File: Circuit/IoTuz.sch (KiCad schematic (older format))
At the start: 35 parts, among them P1 SD_SPI, P2 BATTERY, P3 USB_5PIN_SHELL, P4 LED_1, P5 LED_2, P6 CONN_01X20, P7 CONN_01X20, P8 LCD_SCREEN, Q1 S8050, Q2 S8050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

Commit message: Moved LXDC2XQ location
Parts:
- P8: footprint (none) -> libs:QDTech-3.2in-TFT
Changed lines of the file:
@@
 F 0 "P8" H 9150 4250 50  0000 C CNN
 F 1 "LCD_SCREEN" V 9250 3500 50  0000 C CNN
-F 2 "" H 9150 3500 50  0001 C CNN
+F 2 "libs:QDTech-3.2in-TFT" H 9150 3500 50  0001 C CNN
 F 3 "" H 9150 3500 50  0000 C CNN
 	1    9150 3500

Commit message: Added footprint for LCD.
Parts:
- removed P1: SD_SPI, symbol CONN_01X04
- removed P8: LCD_SCREEN, libs:QDTech-3.2in-TFT, symbol CONN_01X14
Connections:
- net labels removed: CS, D/C, LED, RESET, SCK, SDI(MOSI), SDO(MISO), SD_CS, SD_MISO, SD_MOSI, SD_SCK, T_CLK, T_CS, T_DIN, T_DO, T_IRQ
- wire segments 232 -> 213
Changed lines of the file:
@@
 LIBS:bme280
 LIBS:lxdc2xq
+LIBS:qdtech-3.2-tft
 LIBS:IoTuz-cache
 EELAYER 25 0
@@
 Wire Wire Line
 	2250 2150 2250 1500
-$Comp
-L CONN_01X14 P8
-U 1 1 581185F0
-P 9150 3500
-F 0 "P8" H 9150 4250 50  0000 C CNN
-F 1 "LCD_SCREEN" V 9250 3500 50  0000 C CNN
-F 2 "libs:QDTech-3.2in-TFT" H 9150 3500 50  0001 C CNN
-F 3 "" H 9150 3500 50  0000 C CNN
-	1    9150 3500
-	-1   0    0    -1
-$EndComp
-$Comp
-L CONN_01X04 P1
-U 1 1 58119106
-P 9150 2350
-F 0 "P1" H 9150 2600 50  0000 C CNN
-F 1 "SD_SPI" V 9250 2350 50  0000 C CNN
-F 2 "" H 9150 2350 50  0001 C CNN
-F 3 "" H 9150 2350 50  0000 C CNN
-	1    9150 2350
-	-1   0    0    -1
-$EndComp
-Wire Wire Line
-	9350 2200 9800 2200
-Text Label 9800 2200 2    60   ~ 0
-SD_CS
-Wire Wire Line
-	9350 2300 9800 2300
-Wire Wire Line
-	9800 2400 9350 2400
-Wire Wire Line
-	9800 2500 9350 2500
-Text Label 9800 2300 2    60   ~ 0
-SD_MOSI
-Text Label 9800 2400 2    60   ~ 0
-SD_MISO
-Text Label 9800 2500 2    60   ~ 0
-SD_SCK
-Wire Wire Line
-	9350 2850 9800 2850
-Wire Wire Line
-	9350 2950 9800 2950
-Wire Wire Line
-	9350 3050 9800 3050
-Wire Wire Line
-	9350 3150 9800 3150
-Wire Wire Line
-	9350 3250 9800 3250
-Wire Wire Line
-	9350 3350 9800 3350
-Wire Wire Line
-	9350 3450 9800 3450
-Wire Wire Line
-	9350 3550 9800 3550
-Wire Wire Line
-	9350 3650 9800 3650
-Wire Wire Line
-	9350 3750 9800 3750
-Wire Wire Line
-	9350 3850 9800 3850
-Wire Wire Line
-	9350 3950 9800 3950
-Wire Wire Line
-	9350 4150 9650 4150
-Text Label 9800 2850 2    60   ~ 0
-T_IRQ
-Text Label 9800 2950 2    60   ~ 0
-T_DO
-Text Label 9800 3050 2    60   ~ 0
-T_DIN
-Text Label 9800 3150 2    60   ~ 0
-T_CS
-Text Label 9800 3250 2    60   ~ 0
-T_CLK
-Text Label 9800 3350 2    60   ~ 0
-SDO(MISO)
-Text Label 9800 3450 2    60   ~ 0
-LED
-Text Label 9800 3550 2    60   ~ 0
-SCK
-Text Label 9800 3650 2    60   ~ 0
-SDI(MOSI)
-Text Label 9800 3750 2    60   ~ 0
-D/C
-Text Label 9800 3850 2    60   ~ 0
-RESET
-Text Label 9800 3950 2    60   ~ 0
-CS
-$Comp
-L GND #PWR030
-U 1 1 58121E66
-P 9500 4250
-F 0 "#PWR030" H 9500 4000 50  0001 C CNN
-F 1 "GND" H 9500 4100 50  0000 C CNN
-F 2 "" H 9500 4250 50  0000 C CNN
-F 3 "" H 9500 4250 50  0000 C CNN
-	1    9500 4250
-	1    0    0    -1
-$EndComp
-$Comp
-L +3.3V #PWR031
-U 1 1 58121F10
-P 9650 4150
-F 0 "#PWR031" H 9650 4000 50  0001 C CNN
-F 1 "+3.3V" H 9650 4290 50  0000 C CNN
-F 2 "" H 9650 4150 50  0000 C CNN
-F 3 "" H 9650 4150 50  0000 C CNN
-	1    9650 4150
-	1    0    0    -1
-$EndComp
-Wire Wire Line
-	9350 4050 9500 4050
-Wire Wire Line
-	9500 4050 9500 4250
 $Sheet
 S 1000 3850 850  500
@@
 $EndSheet
 $Sheet
-S 7300 3700 1100 1300
+S 9300 3300 1100 1300
 U 5811E13F
 F0 "LCDTouch" 60

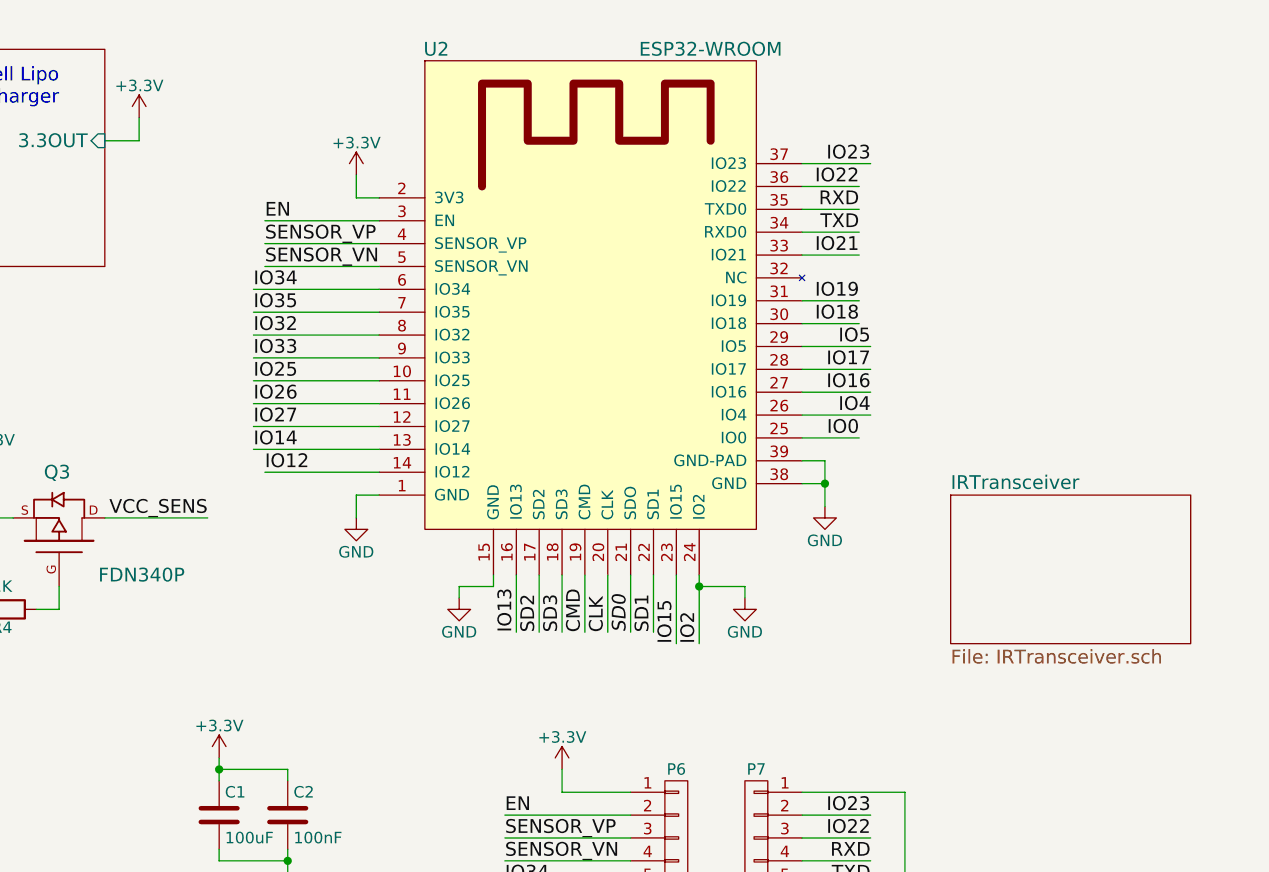
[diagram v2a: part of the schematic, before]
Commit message: Markup IO allocation & add some datasheets.
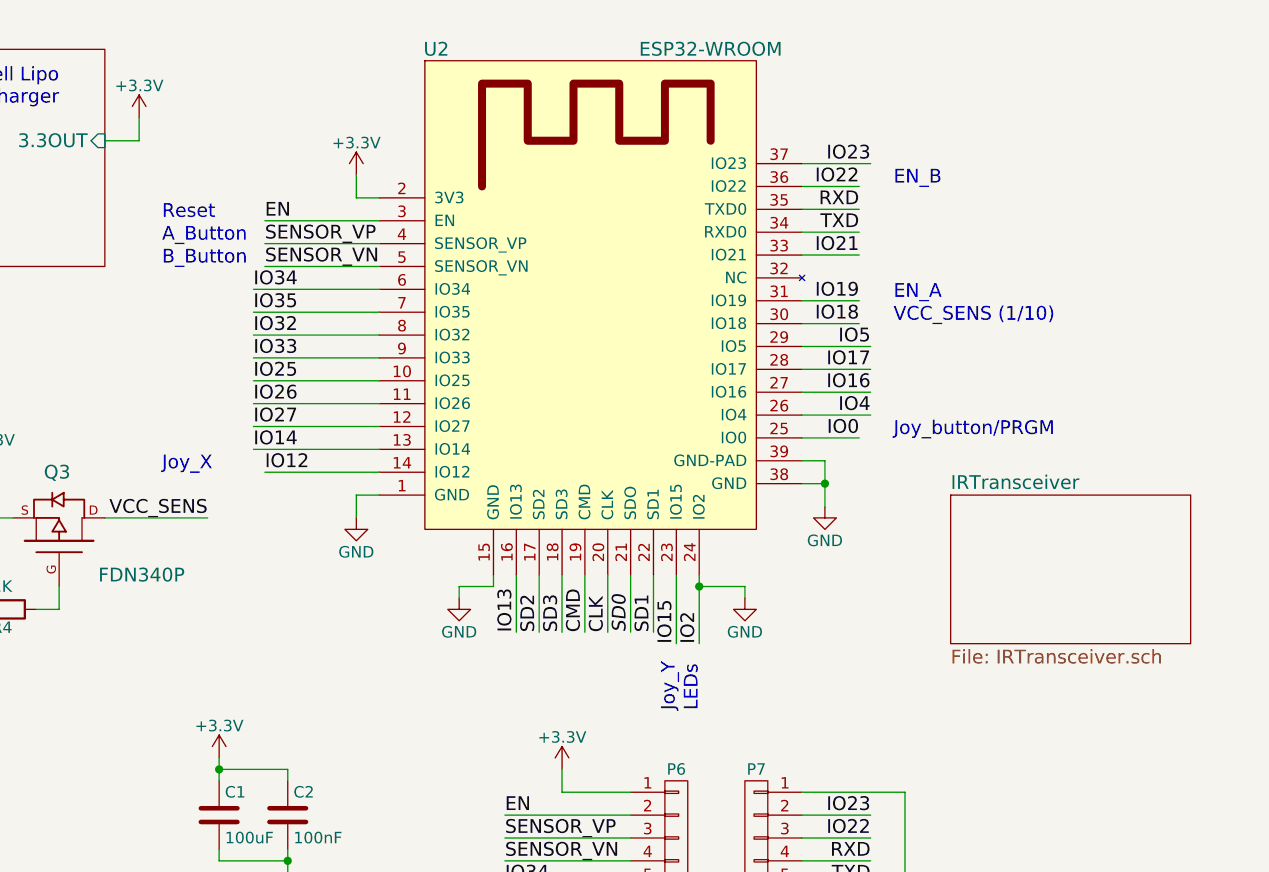
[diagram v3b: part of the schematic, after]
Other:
- note added: "A_Button"
- note added: "B_Button"
- note added: "EN_A"
- note added: "EN_B"
- note added: "Joy_X"
- note added: "Joy_Y"
- note added: "Joy_button/PRGM"
- note added: "LEDs"
- note added: "Reset"
- note added: "VCC_SENS (1/10)"
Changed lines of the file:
@@
 F1 "IRTransceiver.sch" 60
 $EndSheet
+Text Notes 7050 2350 0    60   ~ 0
+Joy_button/PRGM
+Text Notes 7050 1750 0    60   ~ 0
+EN_A
+Text Notes 7050 1250 0    60   ~ 0
+EN_B
+Text Notes 3850 2500 0    60   ~ 0
+Joy_X
+Text Notes 6100 3550 1    60   ~ 0
+Joy_Y
+Text Notes 7050 1850 0    60   ~ 0
+VCC_SENS (1/10)
+Text Notes 3850 1500 0    60   ~ 0
+A_Button
+Text Notes 3850 1600 0    60   ~ 0
+B_Button
+Text Notes 3850 1400 0    60   ~ 0
+Reset
+Text Notes 6200 3550 1    60   ~ 0
+LEDs
 $EndSCHEMATC

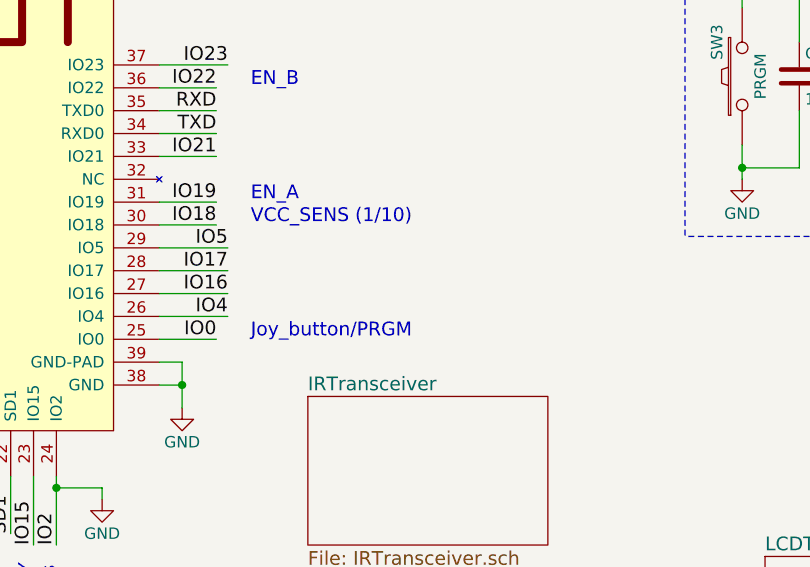
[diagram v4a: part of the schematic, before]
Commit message: Audio choices being narrowed.
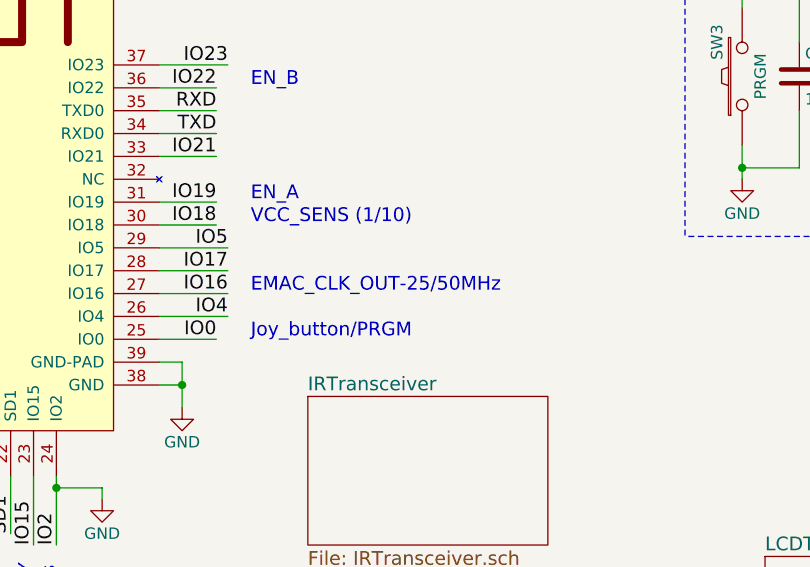
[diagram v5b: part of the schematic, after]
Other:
- note added: "EMAC_CLK_OUT-25/50MHz"
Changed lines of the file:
@@
 Text Notes 6200 3550 1    60   ~ 0
 LEDs
+Text Notes 7050 2150 0    60   ~ 0
+EMAC_CLK_OUT-25/50MHz
 $EndSCHEMATC

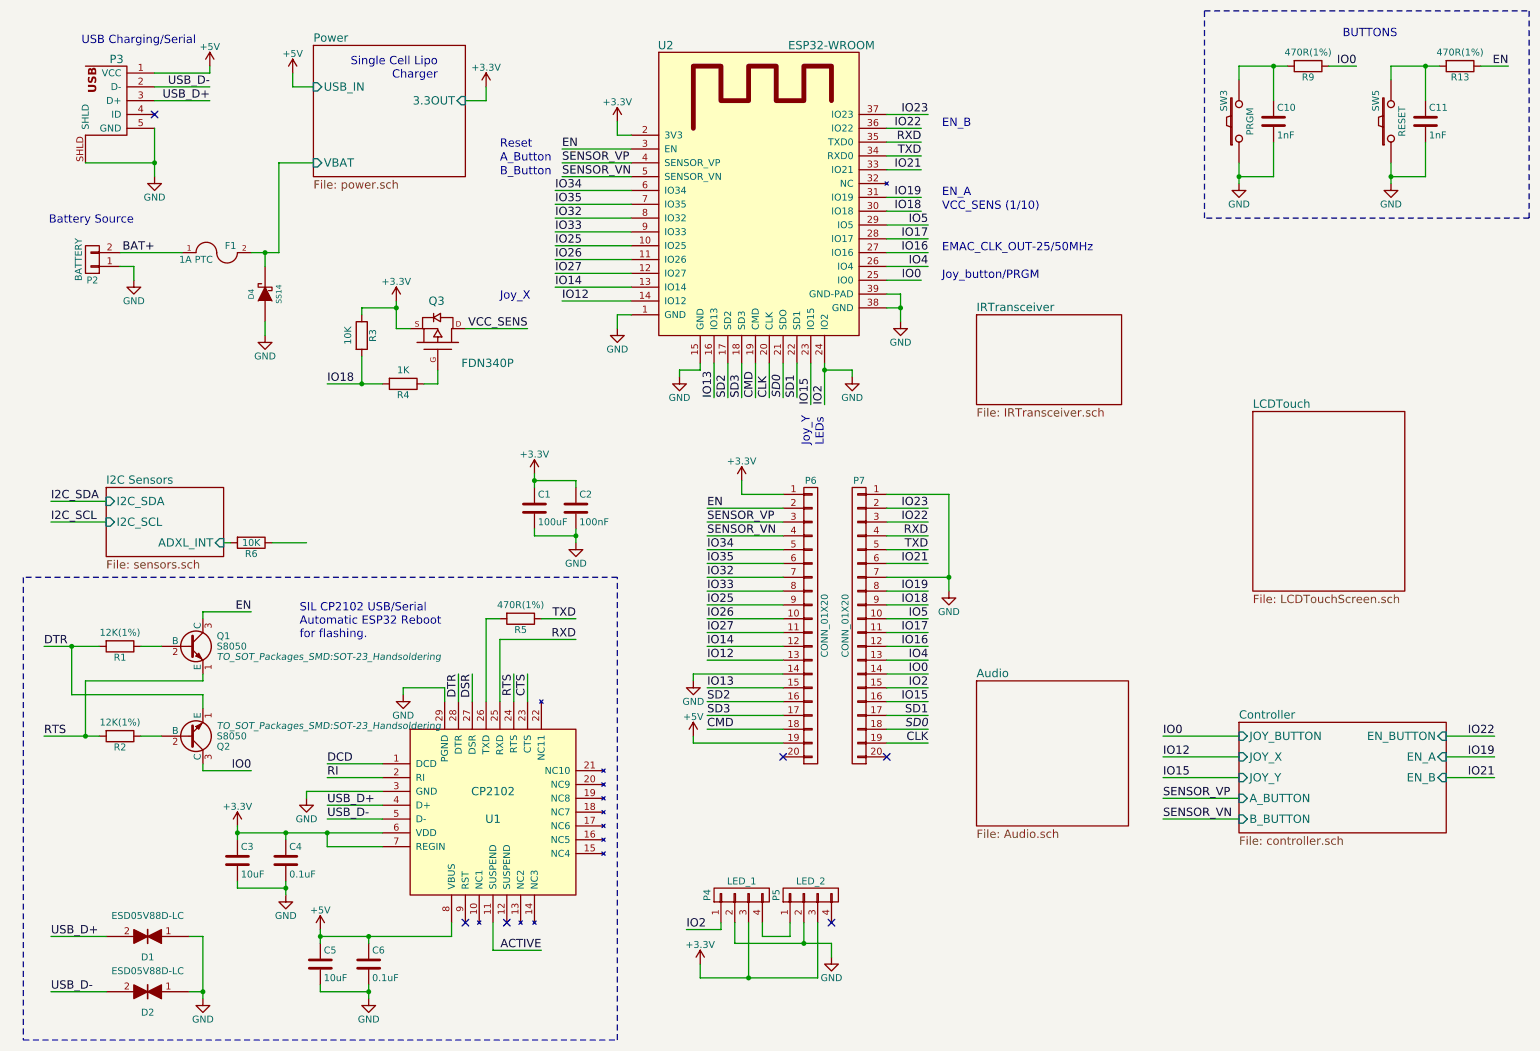
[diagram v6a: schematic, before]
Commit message: Audio hierarchical pins.
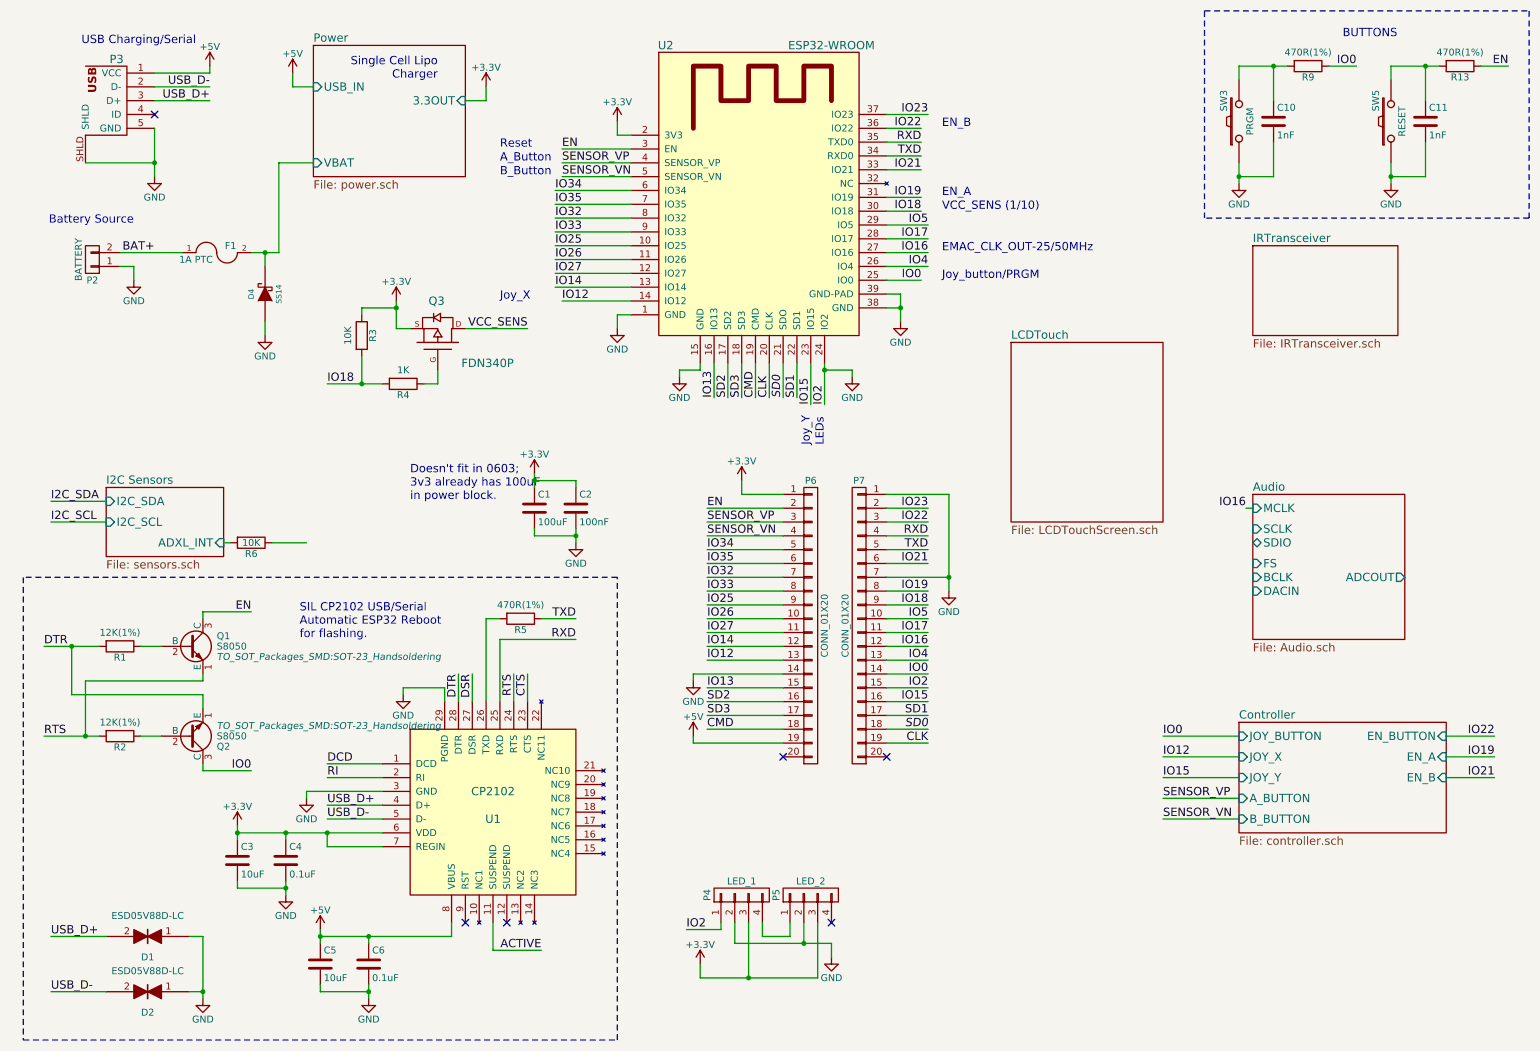
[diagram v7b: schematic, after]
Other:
- note added: "Doesn't fit in 0603;\n3v3 already has 100uF\nin power block."
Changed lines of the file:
@@
 	10700 5950 11050 5950
 $Sheet
-S 7300 5250 1100 1050
+S 9300 3900 1100 1050
 U 5811BE75
 F0 "Audio" 60
 F1 "Audio.sch" 60
+F2 "MCLK" I L 9300 4000 60
+F3 "SCLK" I L 9300 4150 60
+F4 "SDIO" B L 9300 4250 60
+F5 "FS" I L 9300 4400 60
+F6 "BCLK" I L 9300 4500 60
+F7 "DACIN" I L 9300 4600 60
+F8 "ADCOUT" O R 10400 4500 60
 $EndSheet
 $Sheet
-S 9300 3300 1100 1300
+S 7550 2800 1100 1300
 U 5811E13F
 F0 "LCDTouch" 60
@@
 $EndSheet
 $Sheet
-S 7300 2600 1050 650
+S 9300 2100 1050 650
 U 5811E5C9
 F0 "IRTransceiver" 60
@@
 Text Notes 7050 2150 0    60   ~ 0
 EMAC_CLK_OUT-25/50MHz
+Text Notes 3200 3950 0    60   ~ 0
+Doesn't fit in 0603;\n3v3 already has 100uF\nin power block.
+Text Label 9250 4000 2    60   ~ 0
+IO16
+Wire Wire Line
+	9250 4000 9300 4000
 $EndSCHEMATC

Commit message: Removed duplicate stabilizing capacitors.
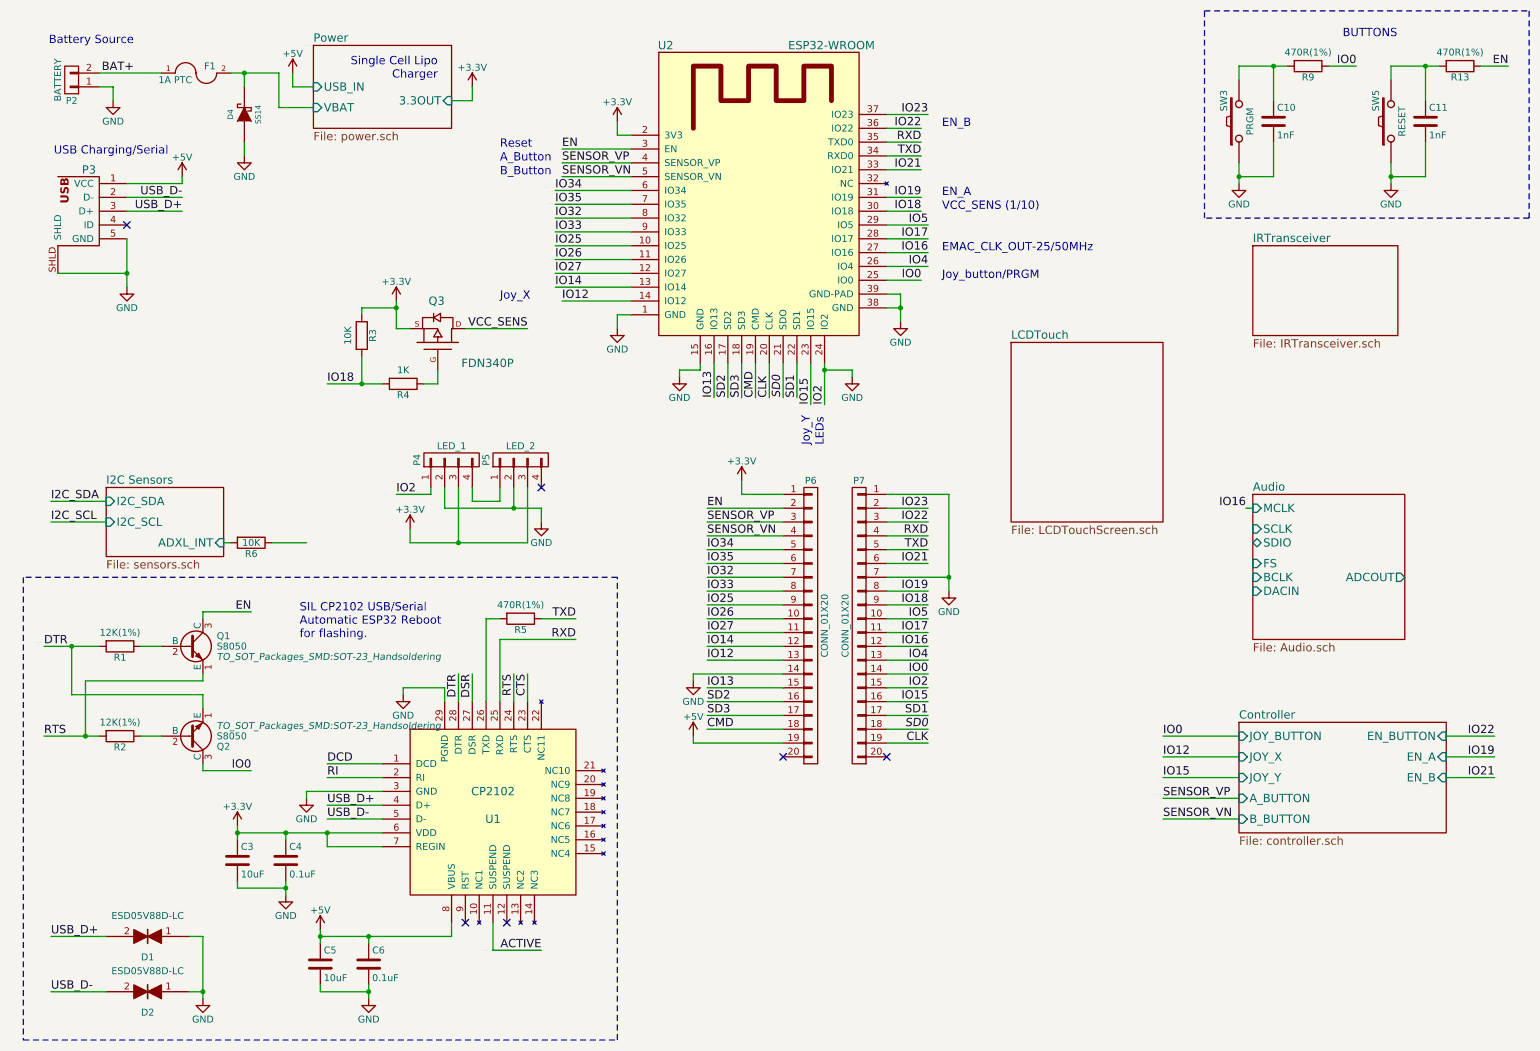
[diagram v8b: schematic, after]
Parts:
- removed C1: 100uF, Capacitors_SMD:C_0603_HandSoldering, symbol C
- removed C2: 100nF, Capacitors_SMD:C_0603_HandSoldering, symbol C
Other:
- note removed: "Doesn't fit in 0603;\n3v3 already has 100uF\nin power block."
- moved on the sheet: D4, F1, P2, P3, P4, P5
